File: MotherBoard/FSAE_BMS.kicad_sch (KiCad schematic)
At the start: 4 parts

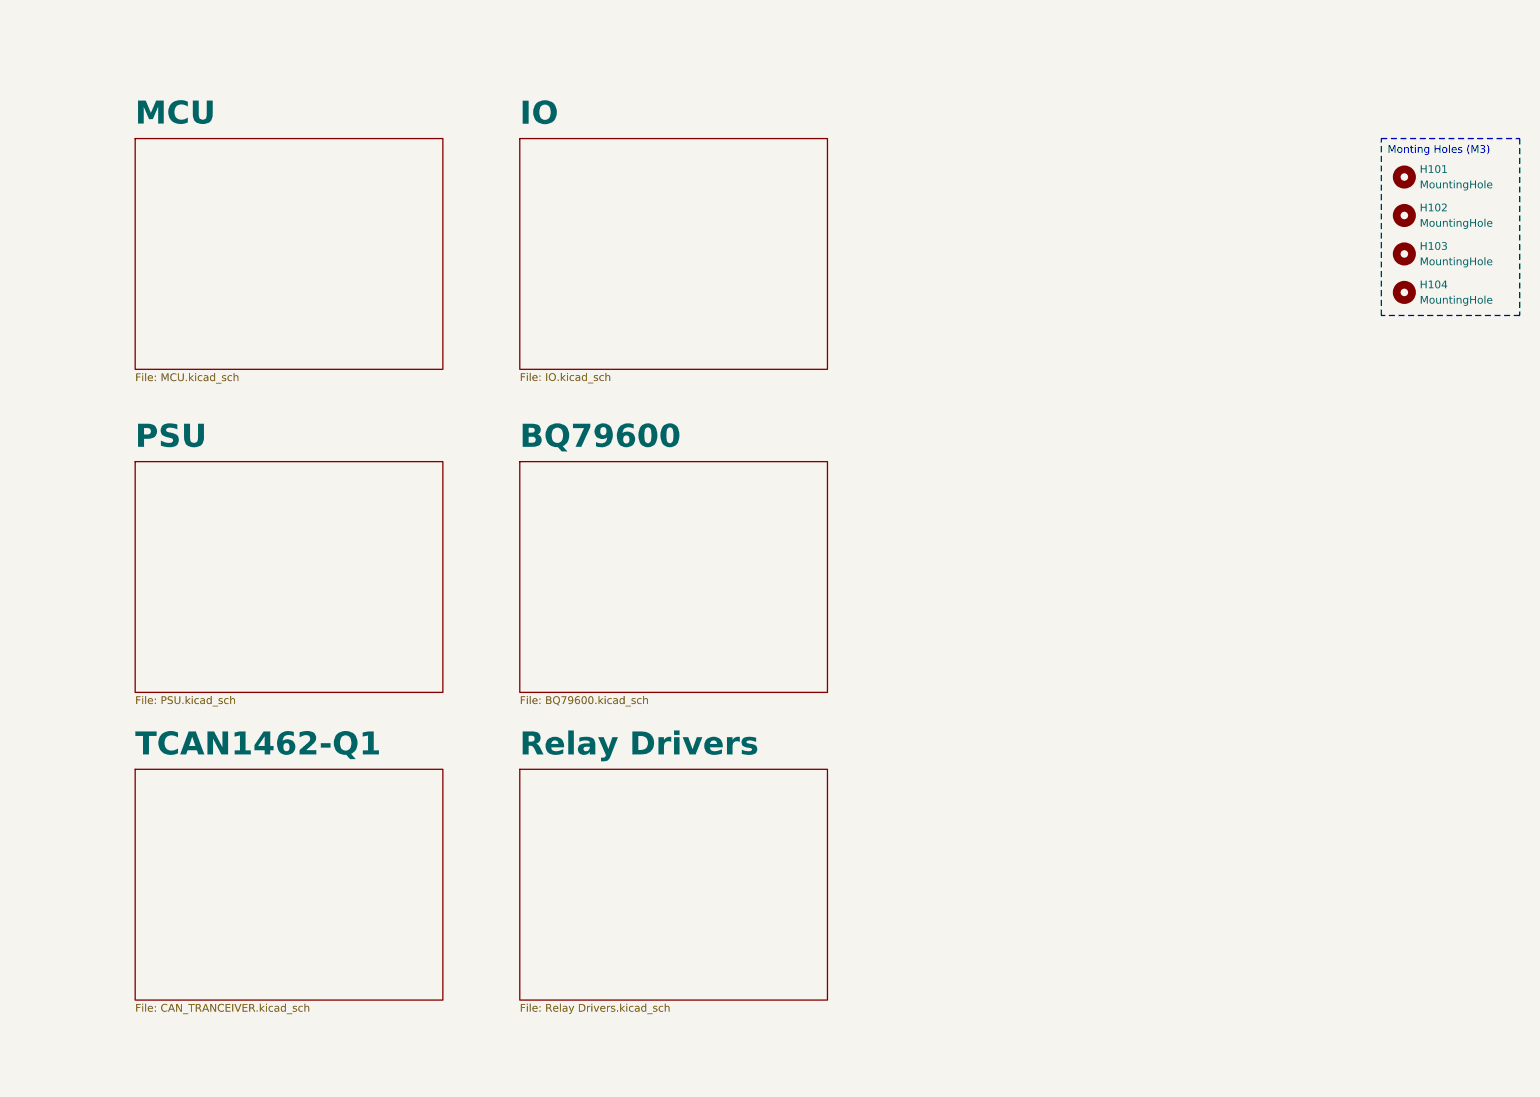
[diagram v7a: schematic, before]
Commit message: Redesigned EMI filters for switching regulators to meet CISPR 25 Class 5 EMI constraint + substituted BOM #s for JLC basic parts
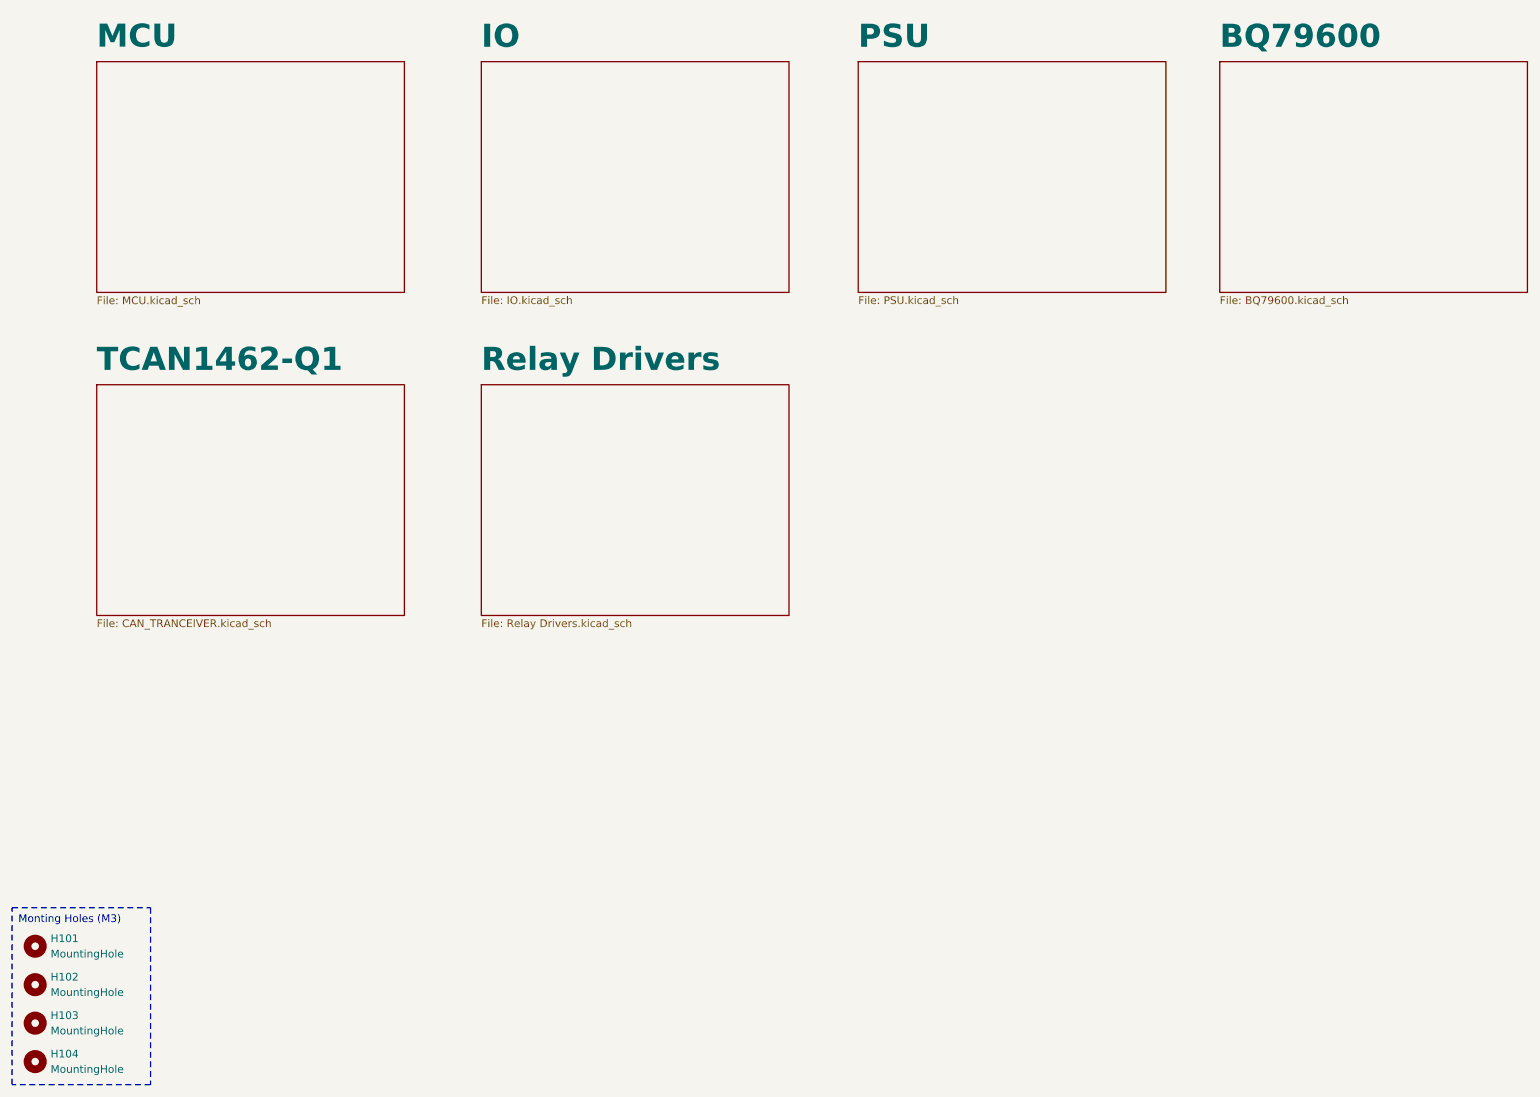
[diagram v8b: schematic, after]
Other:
- moved on the sheet: H101, H102, H103, H104
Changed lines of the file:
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@@
 	(text_box "Monting Holes (M3)"
 		(exclude_from_sim no)
-		(at 243.84 38.1 0)
+		(at 17.78 165.1 0)
 		(size 22.86 29.21)
 		(stroke
@@
 	(symbol
 		(lib_id "Mechanical:MountingHole")
-		(at 247.65 44.45 0)
+		(at 21.59 171.45 0)
 		(unit 1)
 		(exclude_from_sim yes)
@@
 		(fields_autoplaced yes)
 		(property "Reference" "H101"
-			(at 250.19 43.1799 0)
+			(at 24.13 170.1799 0)
 			(effects
 				(font
@@
 		)
 		(property "Value" "MountingHole"
-			(at 250.19 45.7199 0)
+			(at 24.13 172.7199 0)
 			(effects
 				(font
@@
 		)
 		(property "Footprint" "MountingHole:MountingHole_3.2mm_M3"
-			(at 247.65 44.45 0)
+			(at 21.59 171.45 0)
 			(effects
 				(font
@@
 		)
 		(property "Datasheet" "~"
-			(at 247.65 44.45 0)
+			(at 21.59 171.45 0)
 			(effects
 				(font
@@
 		)
 		(property "Description" "Mounting Hole without connection"
-			(at 247.65 44.45 0)
+			(at 21.59 171.45 0)
 			(effects
 				(font
@@
 		)
 		(property "Sim.Device" ""
-			(at 247.65 44.45 0)
+			(at 21.59 171.45 0)
 			(effects
 				(font
@@
 		)
 		(property "Sim.Pins" ""
-			(at 247.65 44.45 0)
+			(at 21.59 171.45 0)
 			(effects
 				(font
@@
 		)
 		(property "Sim.Type" ""
-			(at 247.65 44.45 0)
+			(at 21.59 171.45 0)
 			(effects
 				(font
@@
 	(symbol
 		(lib_id "Mechanical:MountingHole")
-		(at 247.65 50.8 0)
+		(at 21.59 177.8 0)
 		(unit 1)
 		(exclude_from_sim yes)
@@
 		(fields_autoplaced yes)
 		(property "Reference" "H102"
-			(at 250.19 49.5299 0)
+			(at 24.13 176.5299 0)
 			(effects
 				(font
@@
 		)
 		(property "Value" "MountingHole"
-			(at 250.19 52.0699 0)
+			(at 24.13 179.0699 0)
 			(effects
 				(font
@@
 		)
 		(property "Footprint" "MountingHole:MountingHole_3.2mm_M3"
-			(at 247.65 50.8 0)
+			(at 21.59 177.8 0)
 			(effects
 				(font
@@
 		)
 		(property "Datasheet" "~"
-			(at 247.65 50.8 0)
+			(at 21.59 177.8 0)
 			(effects
 				(font
@@
 		)
 		(property "Description" "Mounting Hole without connection"
-			(at 247.65 50.8 0)
+			(at 21.59 177.8 0)
 			(effects
 				(font
@@
 		)
 		(property "Sim.Device" ""
-			(at 247.65 50.8 0)
+			(at 21.59 177.8 0)
 			(effects
 				(font
@@
 		)
 		(property "Sim.Pins" ""
-			(at 247.65 50.8 0)
+			(at 21.59 177.8 0)
 			(effects
 				(font
@@
 		)
 		(property "Sim.Type" ""
-			(at 247.65 50.8 0)
+			(at 21.59 177.8 0)
 			(effects
 				(font
@@
 	(symbol
 		(lib_id "Mechanical:MountingHole")
-		(at 247.65 57.15 0)
+		(at 21.59 184.15 0)
 		(unit 1)
 		(exclude_from_sim yes)
@@
 		(fields_autoplaced yes)
 		(property "Reference" "H103"
-			(at 250.19 55.8799 0)
+			(at 24.13 182.8799 0)
 			(effects
 				(font
@@
 		)
 		(property "Value" "MountingHole"
-			(at 250.19 58.4199 0)
+			(at 24.13 185.4199 0)
 			(effects
 				(font
@@
 		)
 		(property "Footprint" "MountingHole:MountingHole_3.2mm_M3"
-			(at 247.65 57.15 0)
+			(at 21.59 184.15 0)
 			(effects
 				(font
@@
 		)
 		(property "Datasheet" "~"
-			(at 247.65 57.15 0)
+			(at 21.59 184.15 0)
 			(effects
 				(font
@@
 		)
 		(property "Description" "Mounting Hole without connection"
-			(at 247.65 57.15 0)
+			(at 21.59 184.15 0)
 			(effects
 				(font
@@
 		)
 		(property "Sim.Device" ""
-			(at 247.65 57.15 0)
+			(at 21.59 184.15 0)
 			(effects
 				(font
@@
 		)
 		(property "Sim.Pins" ""
-			(at 247.65 57.15 0)
+			(at 21.59 184.15 0)
 			(effects
 				(font
@@
 		)
 		(property "Sim.Type" ""
-			(at 247.65 57.15 0)
+			(at 21.59 184.15 0)
 			(effects
 				(font
@@
 	(symbol
 		(lib_id "Mechanical:MountingHole")
-		(at 247.65 63.5 0)
+		(at 21.59 190.5 0)
 		(unit 1)
 		(exclude_from_sim yes)
@@
 		(fields_autoplaced yes)
 		(property "Reference" "H104"
-			(at 250.19 62.2299 0)
+			(at 24.13 189.2299 0)
 			(effects
 				(font
@@
 		)
 		(property "Value" "MountingHole"
-			(at 250.19 64.7699 0)
+			(at 24.13 191.7699 0)
 			(effects
 				(font
@@
 		)
 		(property "Footprint" "MountingHole:MountingHole_3.2mm_M3"
-			(at 247.65 63.5 0)
+			(at 21.59 190.5 0)
 			(effects
 				(font
@@
 		)
 		(property "Datasheet" "~"
-			(at 247.65 63.5 0)
+			(at 21.59 190.5 0)
 			(effects
 				(font
@@
 		)
 		(property "Description" "Mounting Hole without connection"
-			(at 247.65 63.5 0)
+			(at 21.59 190.5 0)
 			(effects
 				(font
@@
 		)
 		(property "Sim.Device" ""
-			(at 247.65 63.5 0)
+			(at 21.59 190.5 0)
 			(effects
 				(font
@@
 		)
 		(property "Sim.Pins" ""
-			(at 247.65 63.5 0)
+			(at 21.59 190.5 0)
 			(effects
 				(font
@@
 		)
 		(property "Sim.Type" ""
-			(at 247.65 63.5 0)
+			(at 21.59 190.5 0)
 			(effects
 				(font
@@
 	)
 	(sheet
-		(at 101.6 142.24)
+		(at 95.25 78.74)
 		(size 50.8 38.1)
 		(fields_autoplaced yes)
@@
 		)
 		(property "Sheetname" "Relay Drivers"
-			(at 101.6 140.2584 0)
+			(at 95.25 76.7584 0)
 			(effects
 				(font
@@
 		)
 		(property "Sheetfile" "Relay Drivers.kicad_sch"
-			(at 101.6 180.9246 0)
+			(at 95.25 117.4246 0)
 			(effects
 				(font
@@
 	)
 	(sheet
-		(at 38.1 142.24)
+		(at 31.75 78.74)
 		(size 50.8 38.1)
 		(fields_autoplaced yes)
@@
 		)
 		(property "Sheetname" "TCAN1462-Q1"
-			(at 38.1 140.2584 0)
+			(at 31.75 76.7584 0)
 			(effects
 				(font
@@
 		)
 		(property "Sheetfile" "CAN_TRANCEIVER.kicad_sch"
-			(at 38.1 180.9246 0)
+			(at 31.75 117.4246 0)
 			(effects
 				(font
@@
 	)
 	(sheet
-		(at 38.1 38.1)
+		(at 31.75 25.4)
 		(size 50.8 38.1)
 		(fields_autoplaced yes)
@@
 		)
 		(property "Sheetname" "MCU"
-			(at 38.1 36.093 0)
+			(at 31.75 23.393 0)
 			(effects
 				(font
@@
 		)
 		(property "Sheetfile" "MCU.kicad_sch"
-			(at 38.1 76.81 0)
+			(at 31.75 64.11 0)
 			(effects
 				(font
@@
 	)
 	(sheet
-		(at 101.6 91.44)
+		(at 217.17 25.4)
 		(size 50.8 38.1)
 		(fields_autoplaced yes)
@@
 		)
 		(property "Sheetname" "BQ79600"
-			(at 101.6 89.4584 0)
+			(at 217.17 23.4184 0)
 			(effects
 				(font
@@
 		)
 		(property "Sheetfile" "BQ79600.kicad_sch"
-			(at 101.6 130.1246 0)
+			(at 217.17 64.0846 0)
 			(effects
 				(font
@@
 	)
 	(sheet
-		(at 101.6 38.1)
+		(at 95.25 25.4)
 		(size 50.8 38.1)
 		(fields_autoplaced yes)
@@
 		)
 		(property "Sheetname" "IO"
-			(at 101.6 36.1184 0)
+			(at 95.25 23.4184 0)
 			(effects
 				(font
@@
 		)
 		(property "Sheetfile" "IO.kicad_sch"
-			(at 101.6 76.7846 0)
+			(at 95.25 64.0846 0)
 			(effects
 				(font
@@
 	)
 	(sheet
-		(at 38.1 91.44)
+		(at 157.48 25.4)
 		(size 50.8 38.1)
 		(fields_autoplaced yes)
@@
 		)
 		(property "Sheetname" "PSU"
-			(at 38.1 89.4584 0)
+			(at 157.48 23.4184 0)
 			(effects
 				(font
@@
 		)
 		(property "Sheetfile" "PSU.kicad_sch"
-			(at 38.1 130.1246 0)
-			(effects
-				(font
+			(at 157.48 64.0846 0)
+			(effects
+				(font
